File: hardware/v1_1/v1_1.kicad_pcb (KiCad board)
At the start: 2 copper layers, 139 x 99 mm, 86 parts, among them J1 AUDIO IN, J2 MIDI OUT, J3 MIDI IN, J4 MIDI THRU, J5 OUTPUT R, J6 OUTPUT L - MONO, J7 EXP 2, J8 EXP 1, J9 Batt In, SW1 RotaryEncoder_Switch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

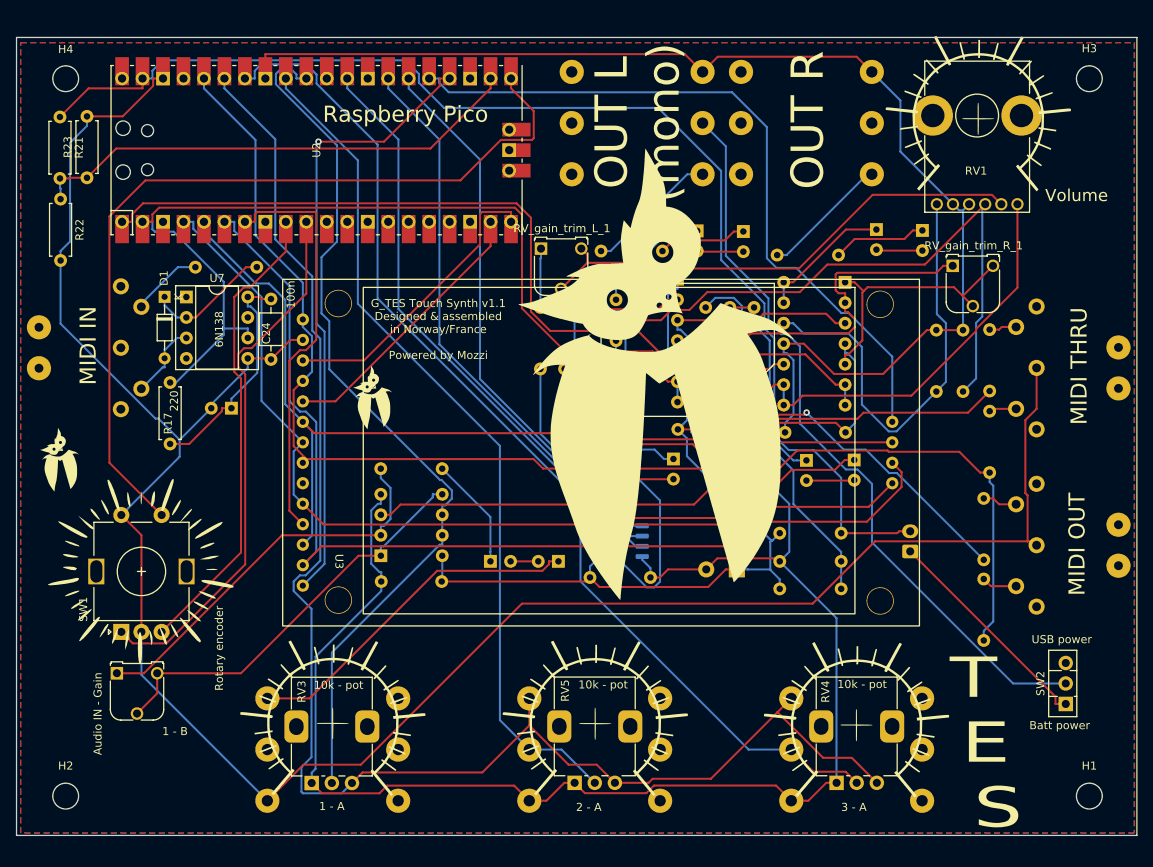
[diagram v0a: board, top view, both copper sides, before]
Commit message: Re-routed pcb for 1.1
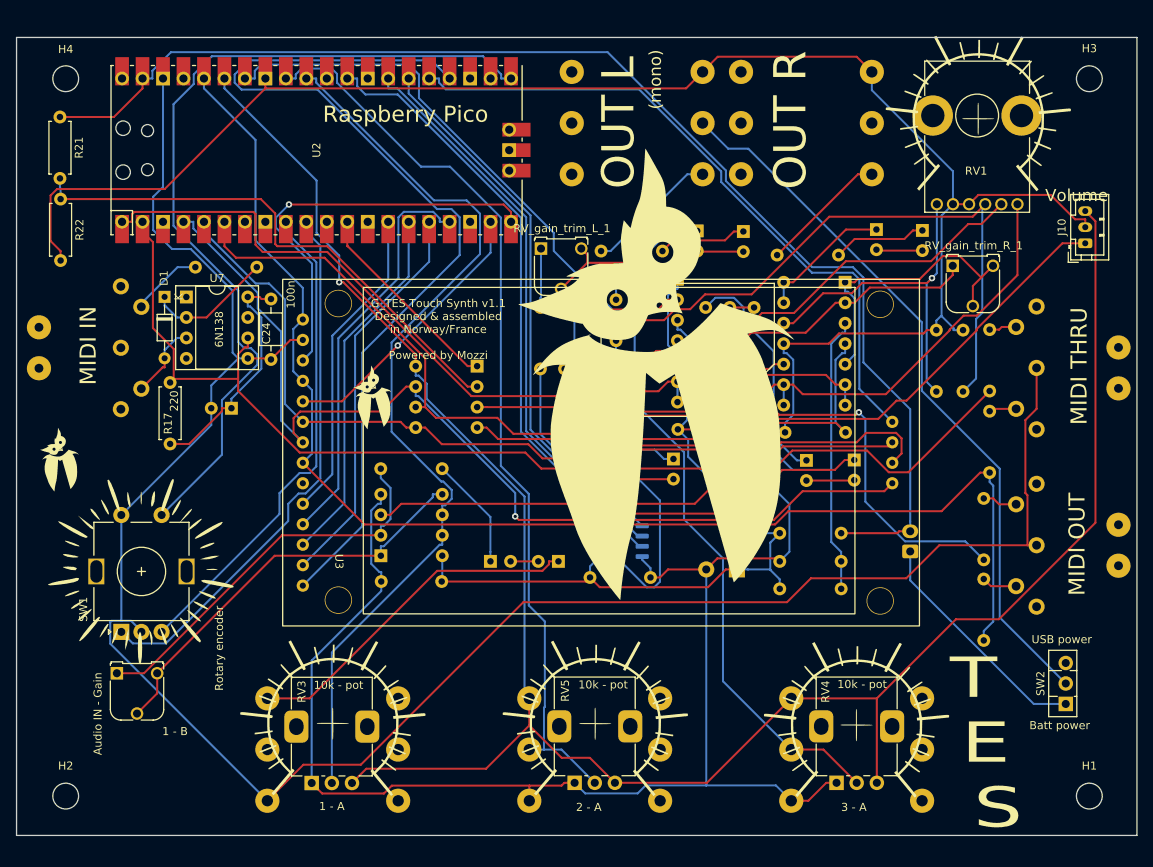
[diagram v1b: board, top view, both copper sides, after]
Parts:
- removed R23: 6.8k, Resistor_THT:R_Axial_DIN0207_L6.3mm_D2.5mm_P7.62mm_Horizontal
- added J10: Additional Sensor, Connector_JST:JST_PH_B3B-PH-K_1x03_P2.00mm_Vertical, F.Cu at (228.1, 66.0)
- added U8: MCP3002, Package_DIP:DIP-8_W7.62mm_Socket, B.Cu at (152.6, 81.3)
- R21: value 10k -> 22k
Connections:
- R22 pad 2: GND -> GNDA
- U2 pad 12: unconnected-(U2-Pad12) -> Net-(U2-Pad12)
- U2 pad 14: unconnected-(U2-Pad14) -> SPI1_CLK
- U2 pad 15: unconnected-(U2-Pad15) -> SPI1_MOSI
- U2 pad 16: unconnected-(U2-Pad16) -> SPI1_MISO
- U2 pad 17: unconnected-(U2-Pad17) -> Net-(U2-Pad17)
- U2 pad 22: Net-(R21-Pad2) -> unconnected-(U2-Pad22)
- U2 pad 4: Net-(U2-Pad4) -> SPI0_CLK
- U2 pad 5: Net-(U2-Pad5) -> SPI0_MOSI
- U2 pad 6: Net-(U2-Pad6) -> SPI0_MISO
- U2 pad 7: Net-(U2-Pad7) -> unconnected-(U2-Pad7)
- U3 pad 10: Net-(U2-Pad4) -> SPI1_CLK
- U3 pad 11: Net-(U2-Pad7) -> Net-(U2-Pad17)
- U3 pad 12: Net-(U2-Pad5) -> SPI1_MOSI
- U3 pad 13: Net-(U2-Pad6) -> SPI1_MISO
- U3 pad 16: Net-(U2-Pad5) -> SPI0_MOSI
- U3 pad 17: Net-(U2-Pad6) -> SPI0_MISO
- U3 pad 18: Net-(U2-Pad4) -> SPI0_CLK
- U3 pad 6: Net-(U2-Pad5) -> SPI0_MOSI
- U3 pad 7: Net-(U2-Pad4) -> SPI0_CLK
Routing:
- net Net-(U2-Pad6): track 130.9 -> 0.00 mm
- net SPI0_CLK: track 0.00 -> 124.7 mm, vias 0 -> 1
- net Net-(U2-Pad5): track 122.8 -> 0.00 mm
- net Net-(U2-Pad4): track 119.1 -> 0.00 mm
- net SPI0_MOSI: track 0.00 -> 108.0 mm
- net SPI0_MISO: track 0.00 -> 107.7 mm
- net Net-(J10-Pad1): track 0.00 -> 85.7 mm
- net ADC_VREF: track 187.6 -> 257.6 mm, vias 0 -> 1
- net GNDA: track 373.9 -> 439.6 mm
- net Net-(U2-Pad7): track 51.1 -> 0.00 mm
- net Net-(U2-Pad17): track 0.00 -> 50.4 mm
- net SPI1_MISO: track 0.00 -> 49.1 mm
- net SPI1_MOSI: track 0.00 -> 45.5 mm
- net Net-(U2-Pad24): track 76.8 -> 117.9 mm, vias 1 -> 0
- net SPI1_CLK: track 0.00 -> 39.4 mm
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- removed copper zone on F.Cu, net GND
- removed copper zone on B.Cu, net GNDA
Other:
- board text added: "(mono)"
- board text added: "OUT L"
- board text removed: "OUT L (mono)"

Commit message: Added MIDI over TRS connector
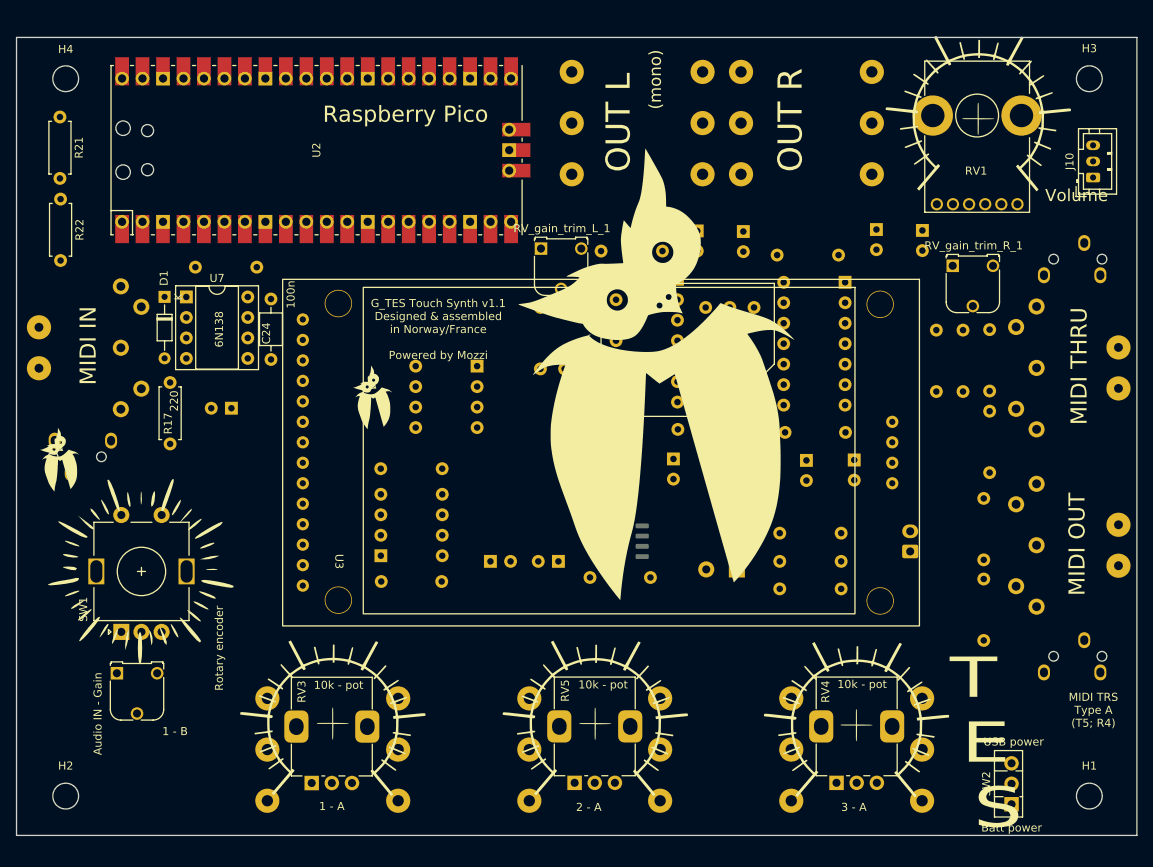
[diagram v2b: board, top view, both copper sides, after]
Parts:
- added J11: MIDI out TRS, MIDI_TRS:PJ-320B, B.Cu at (232.2, 117.3)
- added J12: MIDI in TRS, MIDI_TRS:PJ-320B, B.Cu at (98.0, 92.5)
- added J13: MIDI thru TRS, MIDI_TRS:PJ-320B, B.Cu at (232.2, 68.0)
- moved SW2 14.1 mm to (218.9, 135.6)
- moved J10 8.22 mm to (229.1, 57.9)
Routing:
- net GNDA: track 439.6 -> 0.00 mm
- net ADC_VREF: track 257.6 -> 0.00 mm, vias 1 -> 0
- net GND: track 254.7 -> 0.00 mm
- net +3V3: track 167.2 -> 0.00 mm
- net batt+: track 159.2 -> 0.00 mm
- net Net-(R17-Pad1): track 140.5 -> 0.00 mm
- net Net-(J7-PadR): track 136.6 -> 0.00 mm
- net Net-(R16-Pad1): track 134.9 -> 0.00 mm, vias 1 -> 0
- net SPI0_CLK: track 124.7 -> 0.00 mm, vias 1 -> 0
- net filtered_vcc: track 121.6 -> 0.00 mm
- net Net-(U2-Pad24): track 117.9 -> 0.00 mm
- net virtual_mass: track 117.5 -> 0.00 mm
- net Net-(J8-PadR): track 113.9 -> 0.00 mm
- net Net-(RV3-Pad2): track 113.8 -> 0.00 mm
- net SPI0_MOSI: track 108.0 -> 0.00 mm
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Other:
- board text added: "MIDI TRS Type A (T5; R4)"

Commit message: Routing
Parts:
- moved SW2 14.0 mm to (230.1, 127.1), turned to 180 degrees
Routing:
- net GNDA: track 0.00 -> 442.9 mm
- net ADC_VREF: track 0.00 -> 314.4 mm
- net GND: track 0.00 -> 284.3 mm
- net Net-(R16-Pad1): track 0.00 -> 180.5 mm
- net +3V3: track 0.00 -> 166.3 mm
- net batt+: track 0.00 -> 152.8 mm
- net SPI0_CLK: track 0.00 -> 135.4 mm
- net Net-(J7-PadR): track 0.00 -> 135.4 mm
- net Net-(R17-Pad1): track 0.00 -> 134.9 mm
- net filtered_vcc: track 0.00 -> 121.9 mm
- net Net-(RV3-Pad2): track 0.00 -> 119.3 mm
- net virtual_mass: track 0.00 -> 117.8 mm
- net SPI0_MISO: track 0.00 -> 110.5 mm, vias 0 -> 1
- net Net-(J8-PadR): track 0.00 -> 110.2 mm
- net SPI0_MOSI: track 0.00 -> 107.6 mm
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- added copper zone on F.Cu, net GND
- added copper zone on B.Cu, net GNDA
